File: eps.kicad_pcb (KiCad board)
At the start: 4 copper layers, 95.9 x 90.2 mm, 185 parts, among them J1 PC104-8BIT, J2 PC104PTH, J3 PC104PTH, J4 PC104PTH, J5 PC104PTH, P1 3pin-DC-power, P2 3pin-DC-power, Q10 CSD17551Q3A, Q11 CSD17551Q3A, Q12 CSD17551Q3A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

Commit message: all nets connected
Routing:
- net /VSYS_UP: track 51.5 -> 57.3 mm

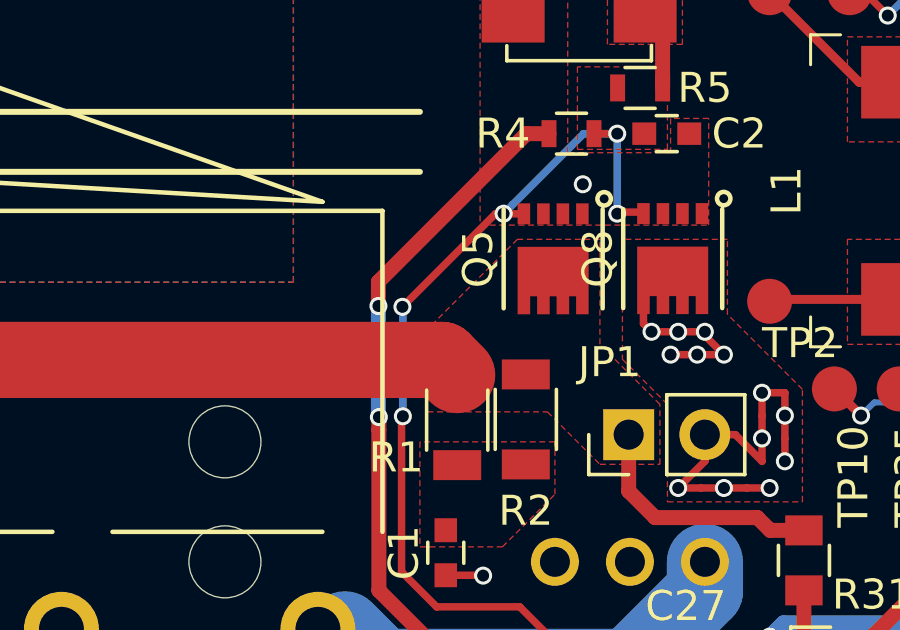
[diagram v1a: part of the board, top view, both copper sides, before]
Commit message: resolved fill related errors
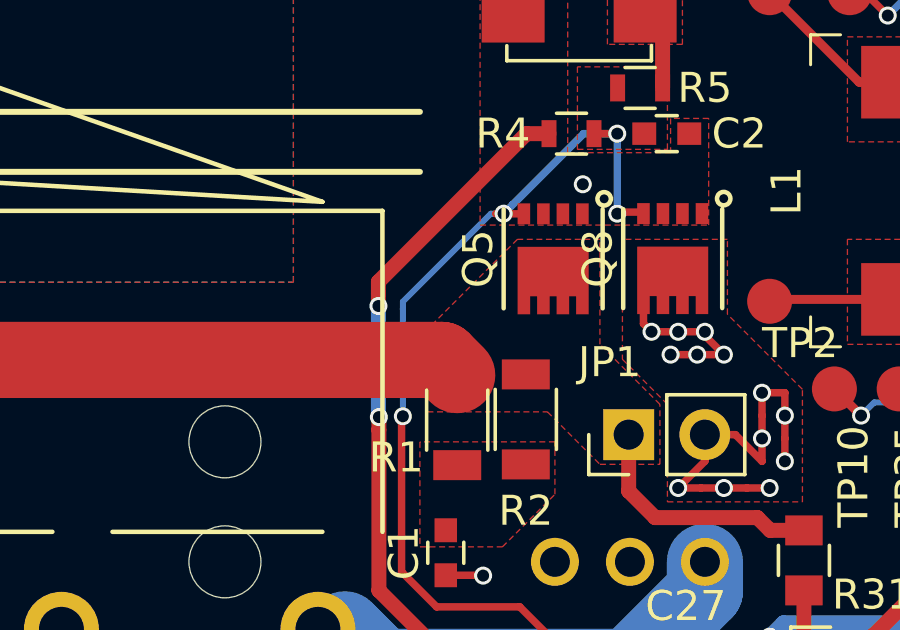
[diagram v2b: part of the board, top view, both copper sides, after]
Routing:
- net Net-(C2-Pad2): track 33.6 -> 34.0 mm, vias 5 -> 4
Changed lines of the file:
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@@
   (general
     (links 445)
-    (no_connects 1)
+    (no_connects 0)
     (area 40.216858 22.899999 491.927847 168.15)
     (thickness 1.6)
@@
   (layers
     (0 F.Cu signal)
-    (1 GND.Cu power hide)
-    (2 PWR.Cu power hide)
-    (31 B.Cu signal hide)
-    (33 F.Adhes user hide)
+    (1 GND.Cu power)
+    (2 PWR.Cu power)
+    (31 B.Cu signal)
+    (33 F.Adhes user)
     (35 F.Paste user)
     (36 B.SilkS user)
@@
   (segment (start 147.303 109.727) (end 146.553 109.727) (width 0.5) (layer F.Cu) (net 45))
   (via (at 141.616619 115.471902) (size 0.6) (drill 0.4) (layers F.Cu B.Cu) (net 45))
-  (segment (start 142.416145 115.49948) (end 145.520914 112.394711) (width 0.25) (layer F.Cu) (net 46))
+  (segment (start 145.788615 112.394711) (end 145.364351 112.394711) (width 0.2) (layer B.Cu) (net 46))
+  (segment (start 145.364351 112.394711) (end 142.431297 115.327765) (width 0.2) (layer B.Cu) (net 46))
+  (segment (start 142.431297 115.327765) (end 142.431297 115.568703) (width 0.2) (layer B.Cu) (net 46))
+  (segment (start 142.431297 119.14899) (end 142.431297 115.568703) (width 0.2) (layer B.Cu) (net 46))
   (segment (start 145.520914 112.394711) (end 145.788615 112.394711) (width 0.25) (layer F.Cu) (net 46))
-  (segment (start 142.431297 119.14899) (end 142.431297 115.514632) (width 0.25) (layer B.Cu) (net 46))
-  (segment (start 142.431297 115.514632) (end 142.416145 115.49948) (width 0.25) (layer B.Cu) (net 46))
-  (via (at 142.416145 115.49948) (size 0.6) (drill 0.4) (layers F.Cu B.Cu) (net 46))
   (segment (start 142.3888 124.333802) (end 142.3888 119.191487) (width 0.25) (layer F.Cu) (net 46))
   (via (at 142.431297 119.14899) (size 0.6) (drill 0.4) (layers F.Cu B.Cu) (net 46))
@@
   )
   (zone (net 105) (net_name /3V3) (layer F.Cu) (hatch edge 0.508)
-    (priority 1)
+    (priority 2)
     (connect_pads yes (clearance 0.2))
     (min_thickness 0.2)

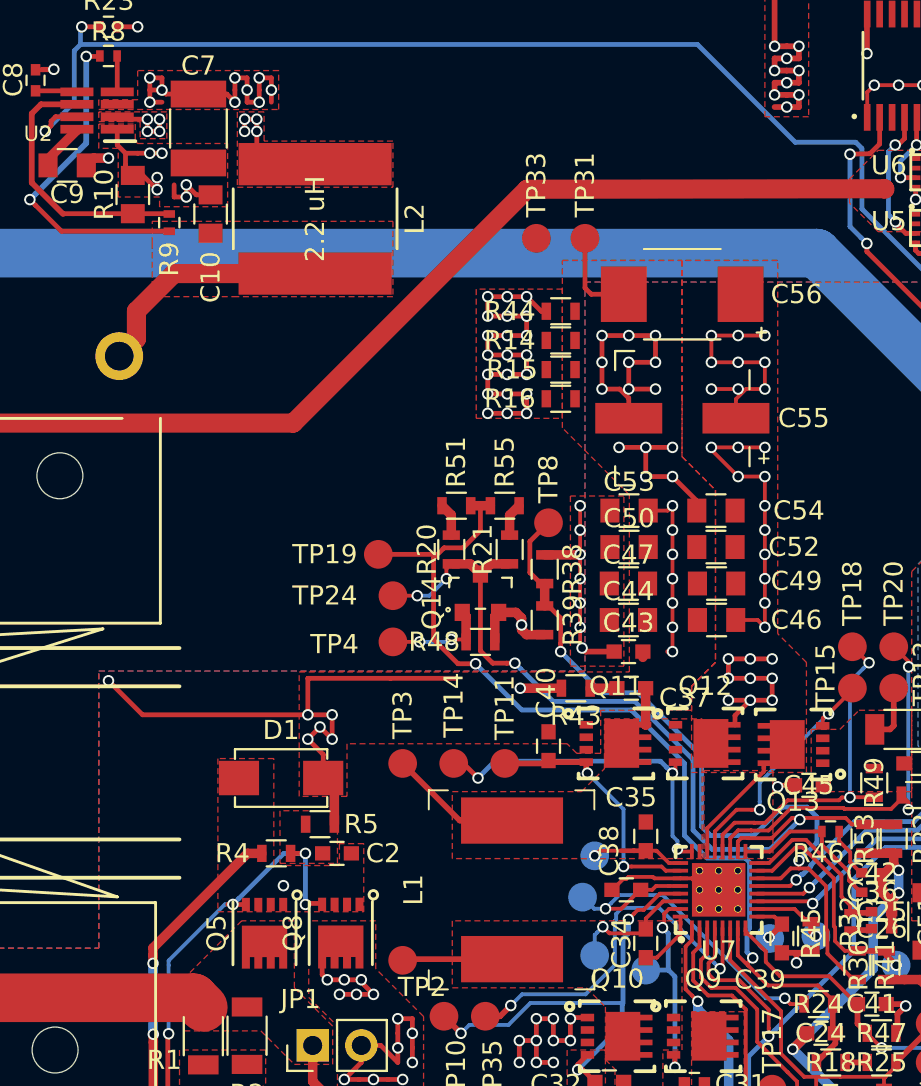
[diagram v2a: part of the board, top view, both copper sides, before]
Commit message: reanamed nets to make layout easier
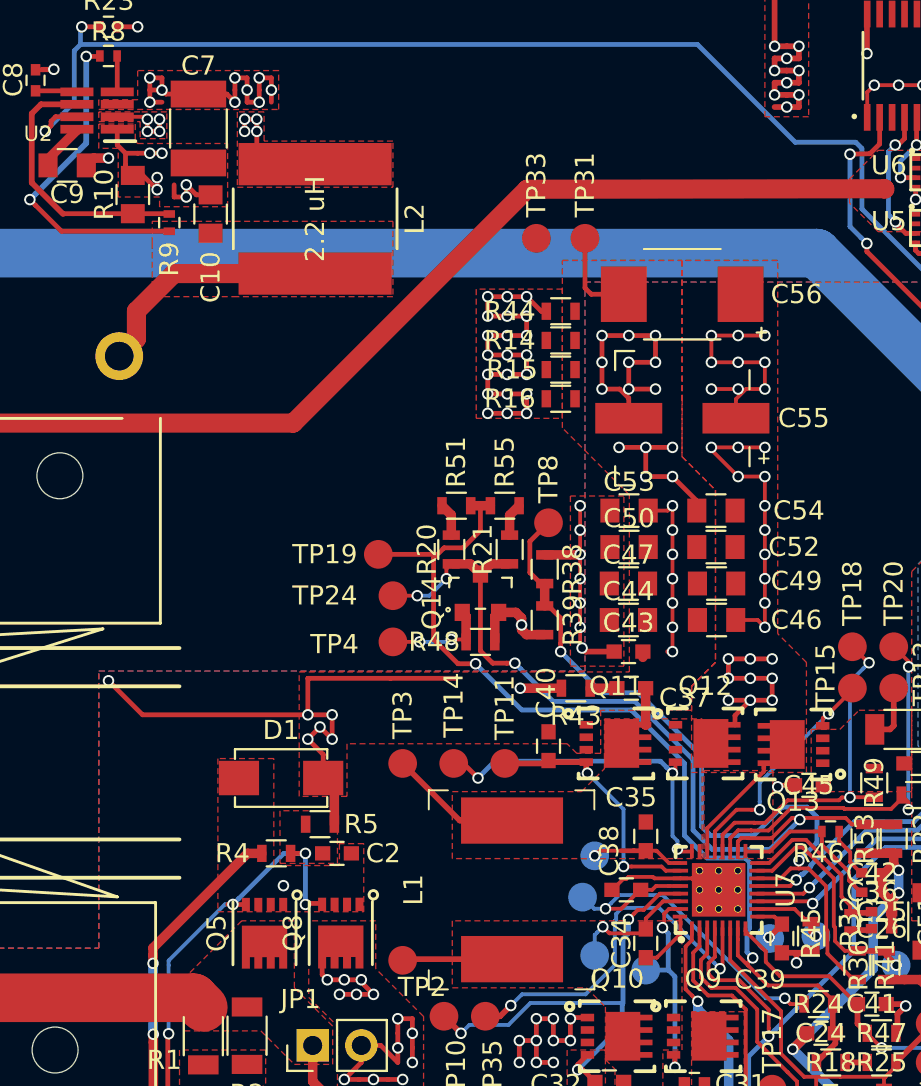
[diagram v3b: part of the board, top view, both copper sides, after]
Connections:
- net Net-(C15-Pad1) renamed /3.3V_Regulator_PDB/BIAS
- net Net-(C16-Pad1) renamed /3.3V_Regulator_PDB/VCC
- net Net-(C22-Pad1) renamed /BMS/ACP
- net Net-(C23-Pad2) renamed /BMS/ACN
- net Net-(C32-Pad1) renamed /BMS/LODRV1
- net Net-(C33-Pad1) renamed /BMS/SW1
- net Net-(C35-Pad1) renamed /BMS/SW2
- net Net-(C36-Pad1) renamed /BMS/COMP2
- net Net-(C40-Pad1) renamed /BMS/LODRV2
- net Net-(C57-Pad1) renamed /3.3V_Regulator_PDB/CBOOT
- net Net-(C57-Pad2) renamed /3.3V_Regulator_PDB/SW
- net Net-(C58-Pad2) renamed /3.3V_Regulator_PDB/FB
- net Net-(C9-Pad1) renamed /1.6A_Regulator_PDB/SW
- net Net-(C9-Pad2) renamed /1.6A_Regulator_PDB/VBOOT
- net Net-(Q12-Pad4) renamed /BMS/HIDRV2
- net Net-(Q9-Pad4) renamed /BMS/HIDRV1
- net Net-(R10-Pad1) renamed /1.6A_Regulator_PDB/FB
- net Net-(R49-Pad2) renamed /BMS/SRP
- net Net-(R54-Pad2) renamed /BMS/SRN
- net Net-(R8-Pad1) renamed /1.6A_Regulator_PDB/PG
- net Net-(U10-Pad4) renamed /PowerDistributionDeploymentControl/on+z
- net Net-(U10-Pad5) renamed /PowerDistributionDeploymentControl/on-z
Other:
- net class Default: clearance 0.2 -> 0.19; trace_width 0.25 -> 0.19
- rule trace_clearance: 0.2 -> 0.19

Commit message: removed reduendent polygon
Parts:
- moved TP33 5.36 mm to (167.0, 77.6)
- moved C9 0.41 mm to (137.1, 74.2)
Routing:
- net /1.6A_Regulator_PDB/1.6A: track 30.3 -> 31.0 mm
- net /PowerDistributionDeploymentControl/1.6A: track 62.7 -> 62.0 mm

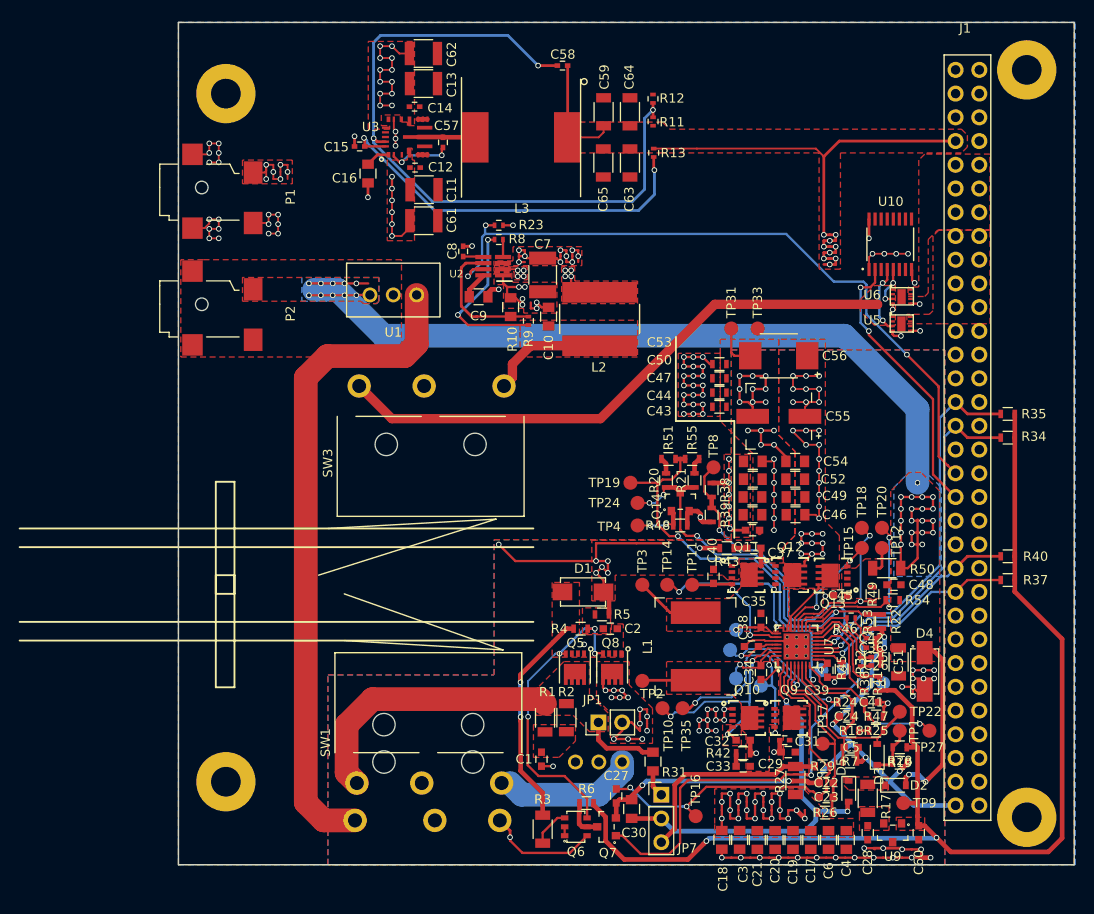
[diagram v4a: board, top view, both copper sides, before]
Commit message: improved high current traces
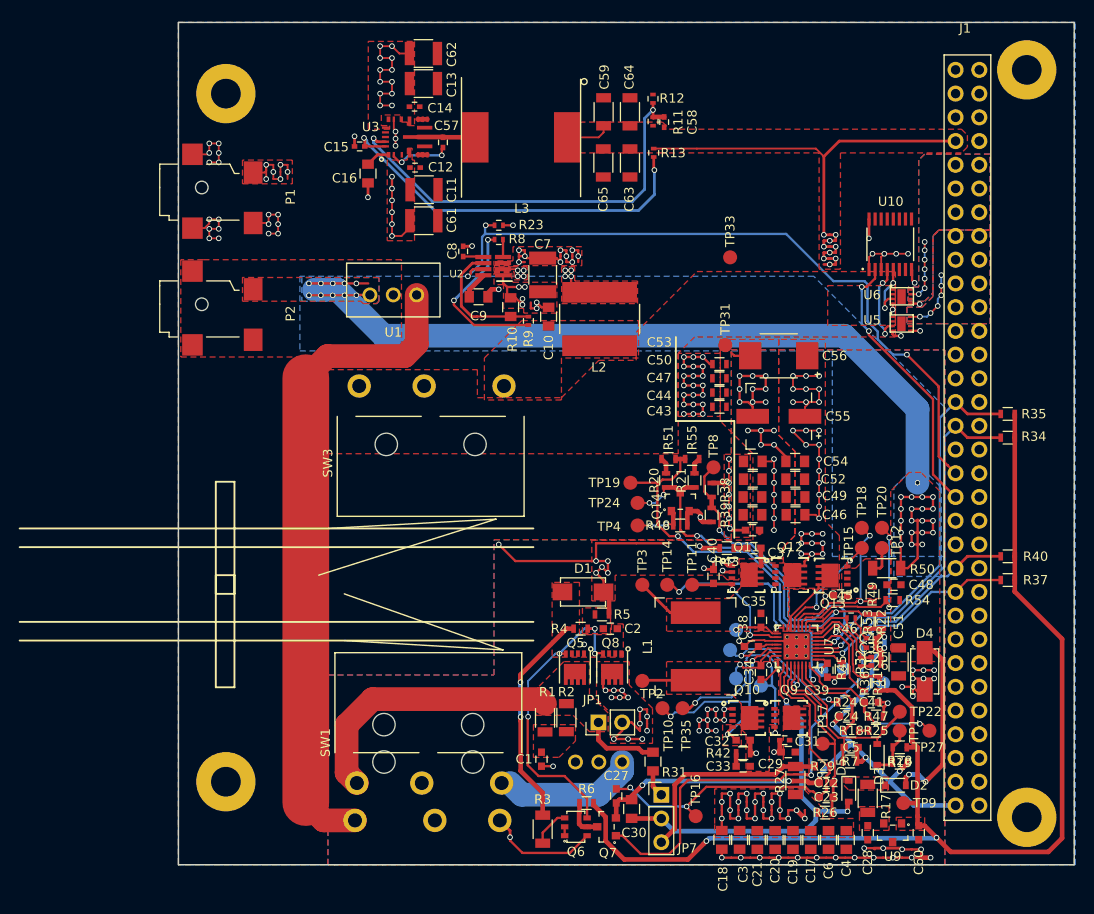
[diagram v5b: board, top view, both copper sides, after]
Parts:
- D4: value DNP -> B220A-13-F
- moved C58 12.5 mm to (157.0, 55.5), turned to 90 degrees
- moved TP33 8.17 mm to (164.1, 70.0)
- moved TP31 1.89 mm to (163.5, 79.4)
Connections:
- C14 pad 2: Net-(C14-Pad2) -> GND
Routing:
- net /PowerDistributionDeploymentControl/1.6A: track 62.0 -> 0.00 mm
- net /3.3V_Regulator_PDB/FB: track 76.1 -> 45.7 mm, vias 3 -> 2
- net /1.6A_Regulator_PDB/1.6A: track 31.0 -> 18.1 mm
- net /3V3: track 69.0 -> 61.4 mm
- net /+z_rail: track 0.00 -> 6.87 mm, vias 0 -> 6
- net /-z_rail: track 0.00 -> 6.75 mm, vias 0 -> 7
- net GNDPWR: track 150.2 -> 153.5 mm, vias 70 -> 76
- net GND: track 151.7 -> 153.5 mm
- net /PowerDistributionDeploymentControl/on-z: track 4.29 -> 6.11 mm
- net /PowerDistributionDeploymentControl/on+z: track 7.37 -> 9.05 mm
- net /DPL_EN: track 76.5 -> 77.5 mm
- added copper zone on B.Cu, net /+z_rail
- added copper zone on B.Cu, net /-z_rail

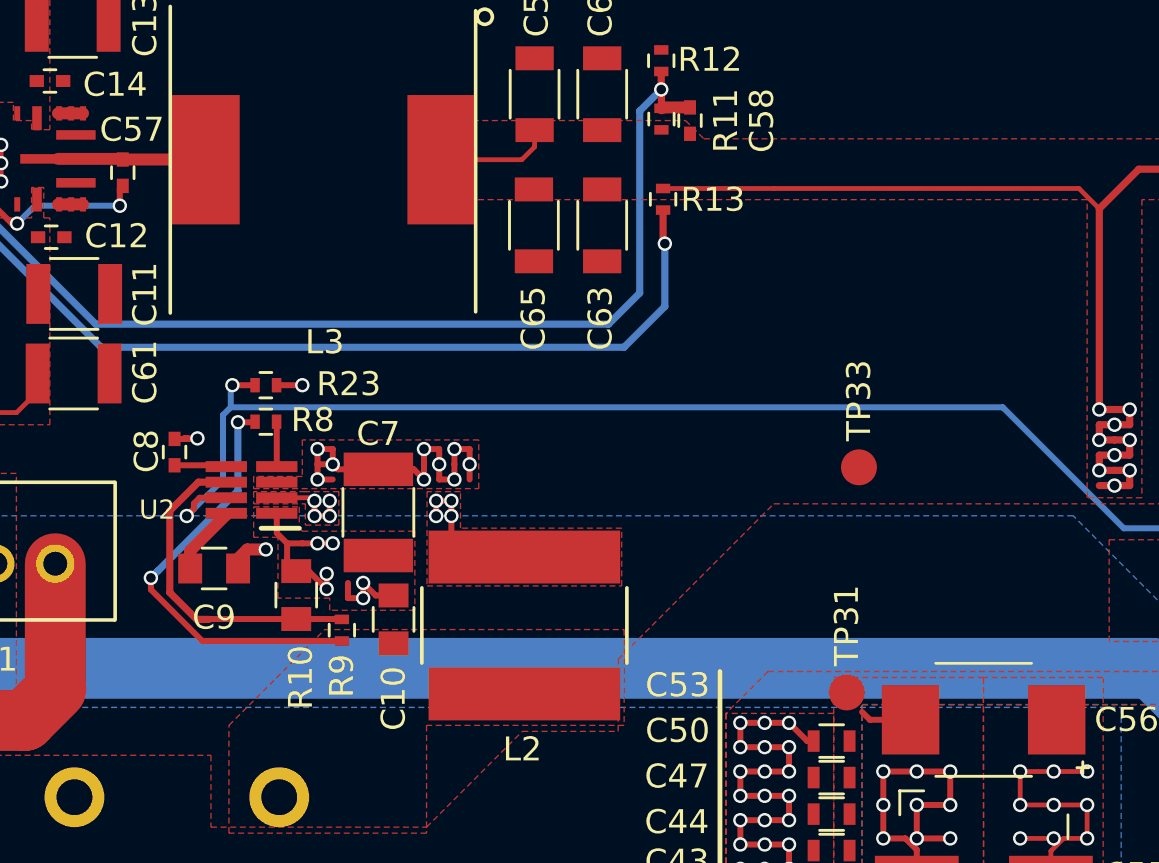
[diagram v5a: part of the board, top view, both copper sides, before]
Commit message: added adjustible feedback for 1.6 a regulator. The point where the feedback taps off moved to after the RBF switch for better control
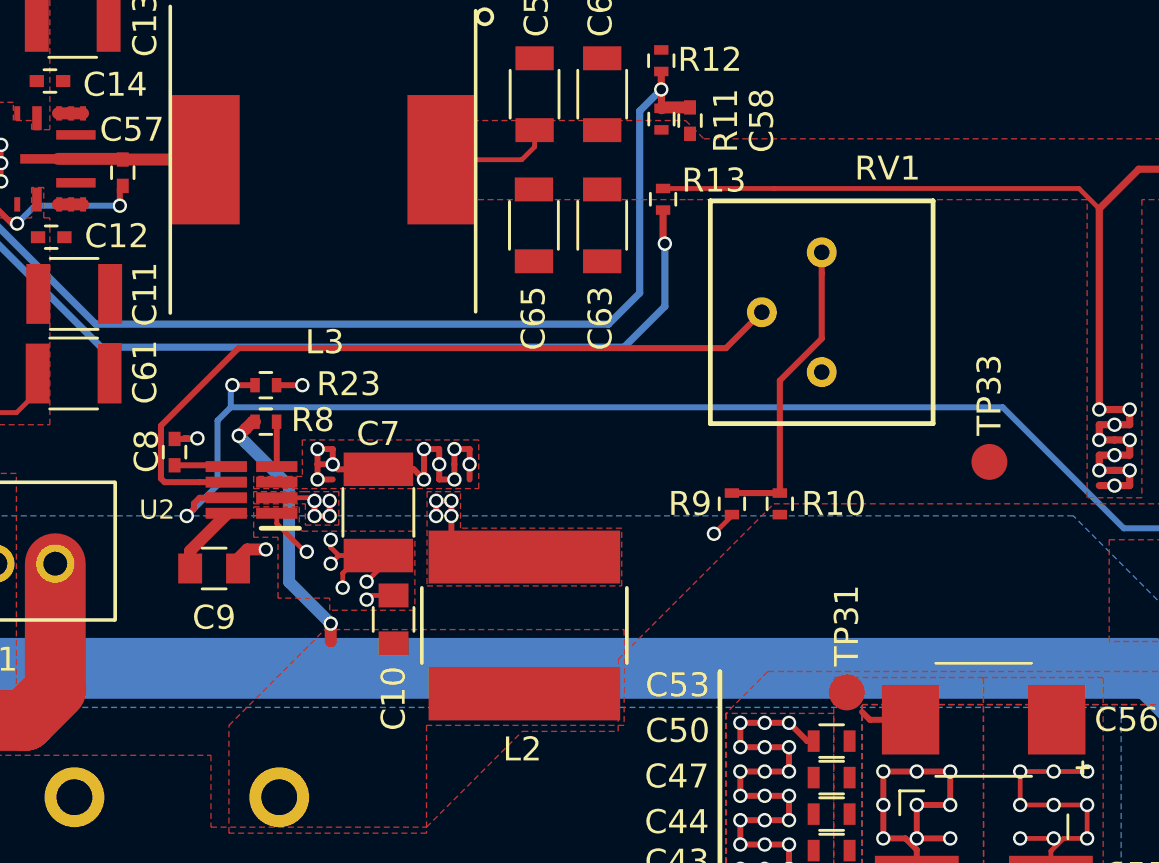
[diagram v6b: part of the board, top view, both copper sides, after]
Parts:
- added RV1: CT6EP103, SFUSat:CT6EP103, F.Cu at (162.5, 63.5)
- R10: value 10.2 kOhm -> 73k2; footprint SFUSat-res:R_0805 -> SFUSat-res:R_0402
- R9: value 34.0 kOhm -> DNP; footprint SFUSat:R_0402 -> SFUSat-res:R_0402
- moved R10 20.5 mm to (160.8, 71.5)
- moved R9 17.1 mm to (158.8, 71.5), turned to 270 degrees
- moved TP33 5.45 mm to (169.5, 69.8)
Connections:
- R10 pad 1: /1.6A_Regulator_PDB/FB -> /PowerDistributionDeploymentControl/1.6A
- R10 pad 2: GND -> Net-(R10-Pad2)
- R9 pad 1: /1.6A_Regulator_PDB/1.6A -> Net-(R10-Pad2)
- R9 pad 2: /1.6A_Regulator_PDB/FB -> GND
- U2 pad 6: /1.6A_Regulator_PDB/FB -> /FB
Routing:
- net /FB: track 0.00 -> 32.0 mm
- net /1.6A_Regulator_PDB/FB: track 13.9 -> 0.00 mm
- net Net-(R10-Pad2): track 0.00 -> 12.8 mm
- net /1.6A_Regulator_PDB/1.6A: track 18.1 -> 11.1 mm
- net GND: track 153.5 -> 154.4 mm, vias 68 -> 69
